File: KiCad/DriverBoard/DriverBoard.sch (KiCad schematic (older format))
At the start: 14 parts, among them J1 Conn_01x11, J2 Conn_01x05, J4 Conn_01x12, Q1 Q_DUAL_NPN_PNP_BRT_E1B1C2E2B2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, Q2 Q_DUAL_NPN_PNP_BRT_E1B1C2E2B2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, Q3 Q_DUAL_NPN_PNP_BRT_E1B1C2E2B2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, Q4 Q_DUAL_NPN_PNP_BRT_E1B1C2E2B2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, Q5 Q_DUAL_NPN_PNP_BRT_E1B1C2E2B2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, Q6 Q_DUAL_NPN_PNP_BRT_E1B1C2E2B2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, Q7 Q_DUAL_NPN_PNP_BRT_E1B1C2E2B2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

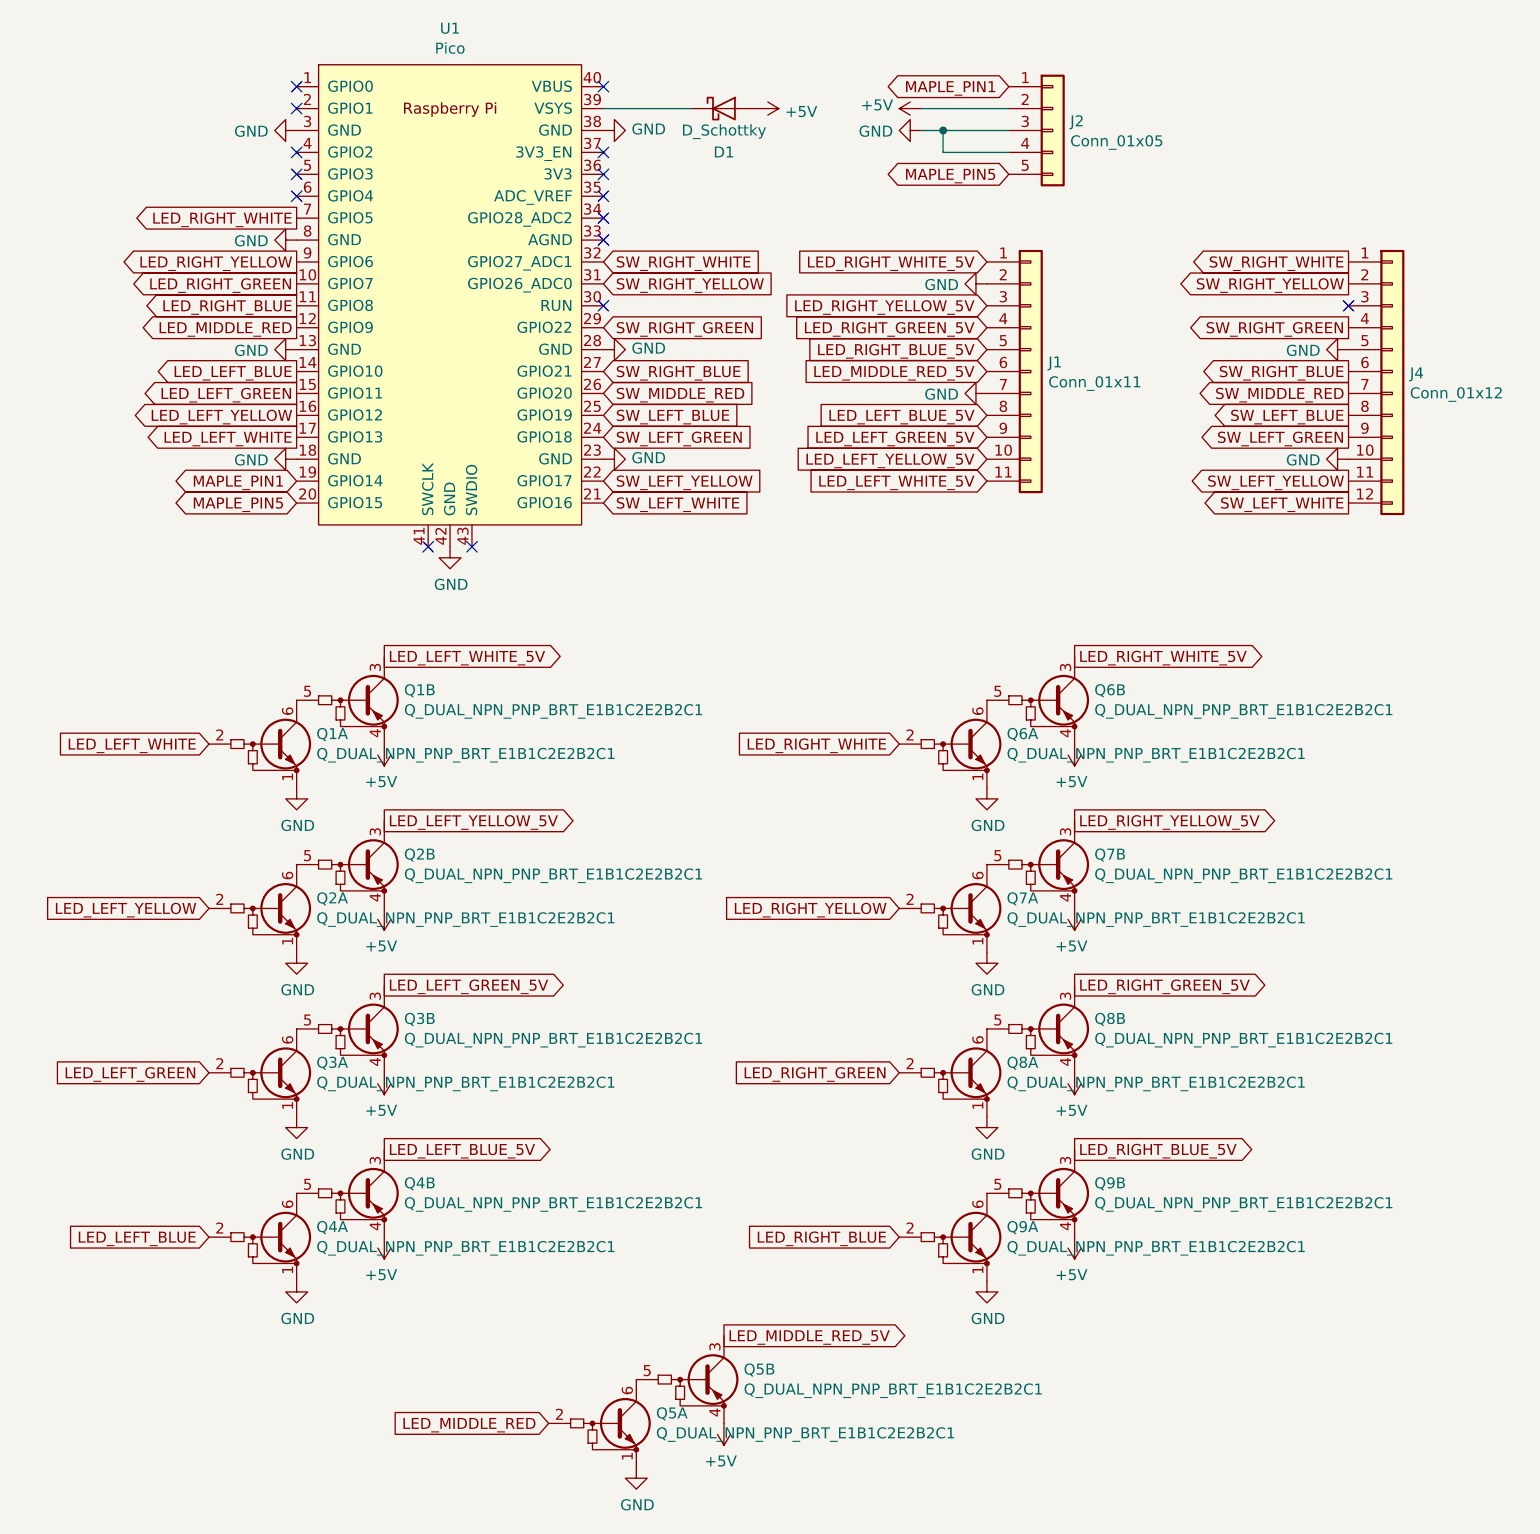
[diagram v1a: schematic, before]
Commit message: Switched misleading silkscreen and updated part numbers
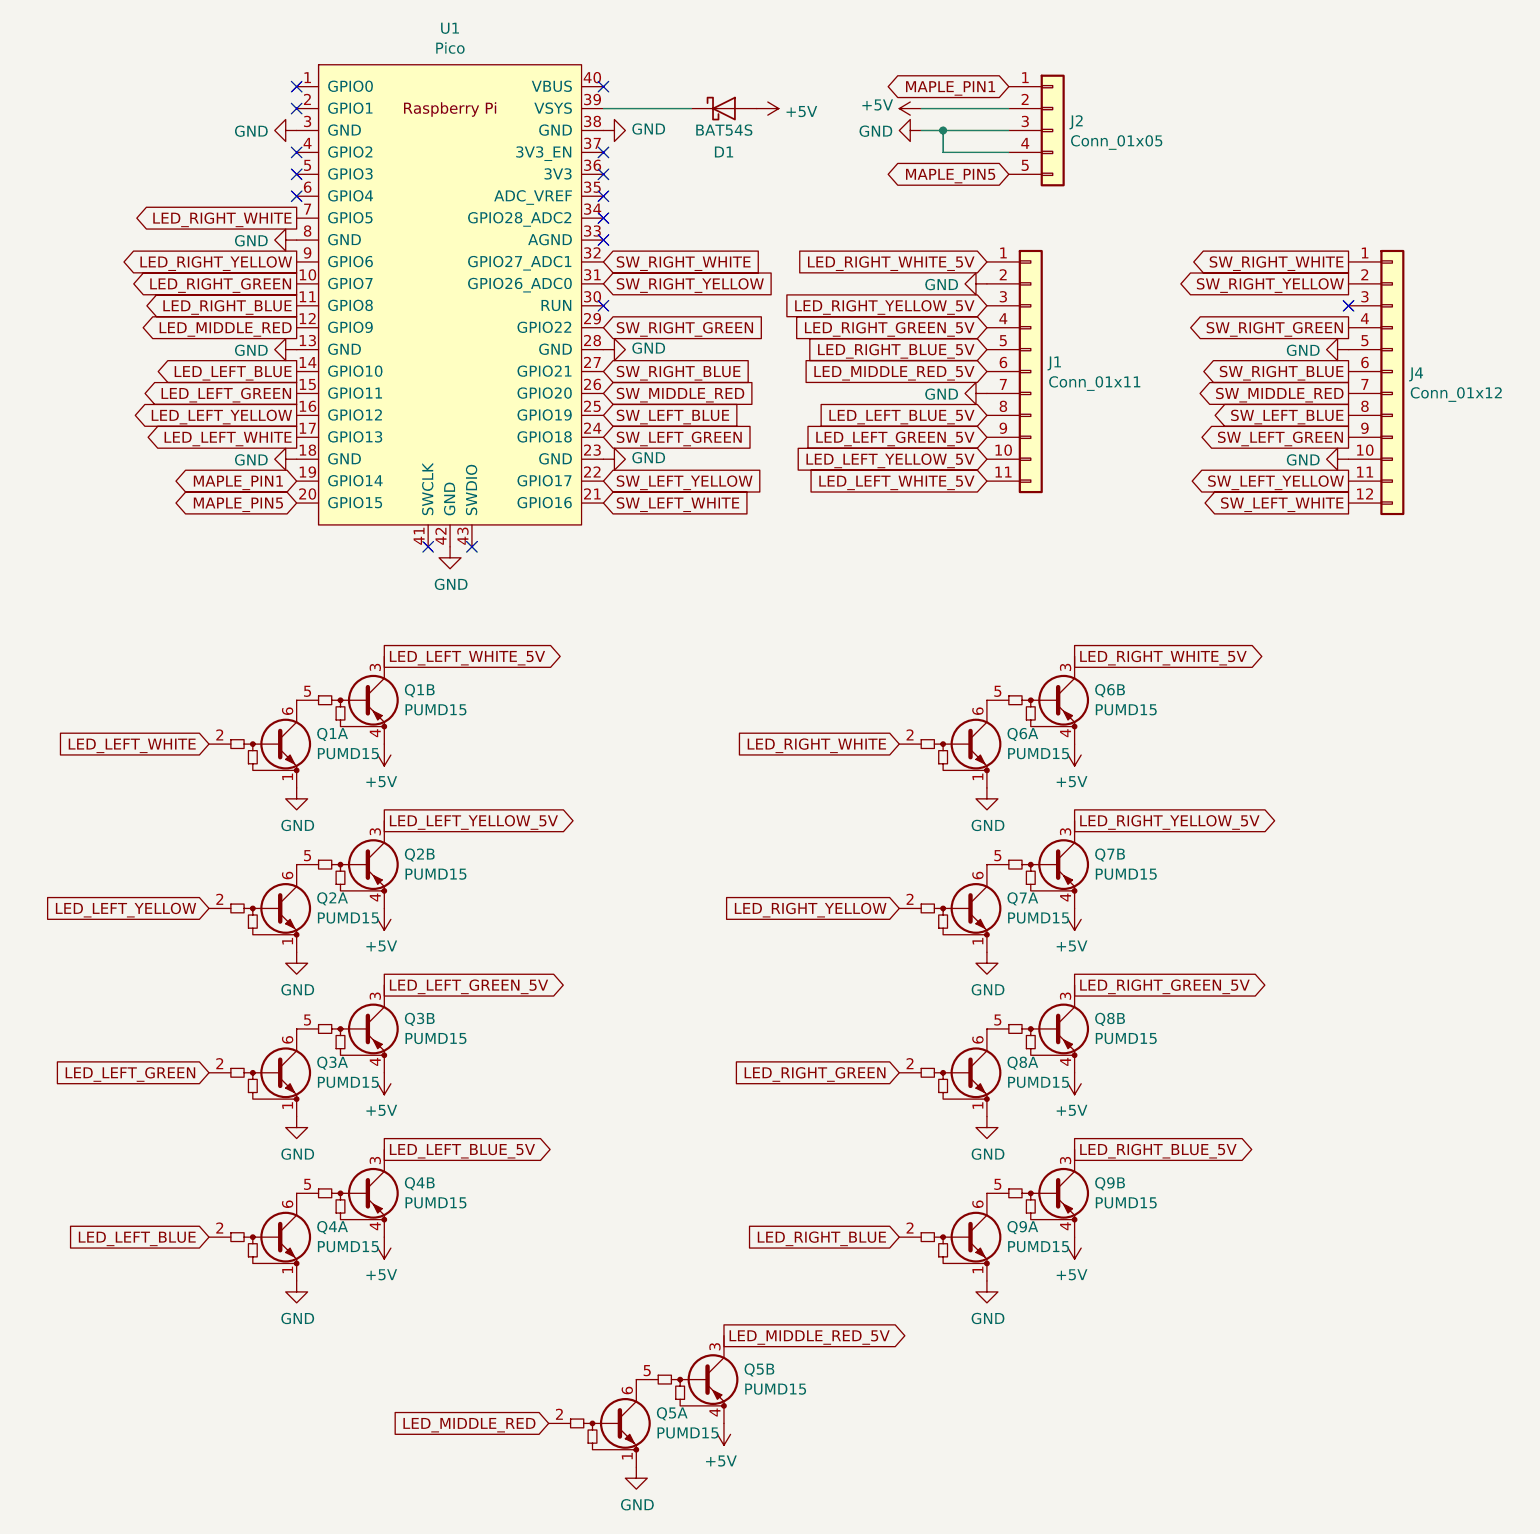
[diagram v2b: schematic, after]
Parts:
- D1: value D_Schottky -> BAT54S
- Q1, Q2, Q3, Q4, Q5, Q6, Q7, Q8, Q9: value Q_DUAL_NPN_PNP_BRT_E1B1C2E2B2C1 -> PUMD15
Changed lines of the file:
@@
 P 3750 1300
 F 0 "D1" H 3750 1100 50  0000 C CNN
-F 1 "D_Schottky" H 3750 1200 50  0000 C CNN
+F 1 "BAT54S" H 3750 1200 50  0000 C CNN
 F 2 "Diode_SMD:D_SOT-23_ANK" H 3750 1300 50  0001 C CNN
-F 3 "~" H 3750 1300 50  0001 C CNN
+F 3 "https://www.vishay.com/docs/85508/bat54.pdf" H 3750 1300 50  0001 C CNN
 	1    3750 1300
 	1    0    0    -1
@@
 NoConn ~ 3200 1200
 $Comp
-L Device:Q_DUAL_NPN_PNP_BRT_E1B1C2E2B2C1 Q1
-U 1 1 6043FA1D
-P 1750 4200
-F 0 "Q1" H 1890 4246 50  0000 L CNN
-F 1 "Q_DUAL_NPN_PNP_BRT_E1B1C2E2B2C1" H 1890 4155 50  0000 L CNN
-F 2 "Package_TO_SOT_SMD:SOT-363_SC-70-6_Handsoldering" H 1750 4200 50  0001 C CNN
-F 3 "~" H 1750 4200 50  0001 C CNN
-	1    1750 4200
-	1    0    0    -1
-$EndComp
-$Comp
 L power:GND #PWR01
 U 1 1 6044CCD8
@@
 LED_LEFT_WHITE_5V
 $Comp
-L Device:Q_DUAL_NPN_PNP_BRT_E1B1C2E2B2C1 Q1
-U 2 1 60452943
-P 2150 4000
-F 0 "Q1" H 2290 4046 50  0000 L CNN
-F 1 "Q_DUAL_NPN_PNP_BRT_E1B1C2E2B2C1" H 2290 3955 50  0000 L CNN
-F 2 "Package_TO_SOT_SMD:SOT-363_SC-70-6_Handsoldering" H 2150 4000 50  0001 C CNN
-F 3 "~" H 2150 4000 50  0001 C CNN
-	2    2150 4000
-	1    0    0    -1
-$EndComp
-$Comp
 L power:GND #PWR02
 U 1 1 6045294F
@@
 P 1750 6450
 F 0 "Q4" H 1890 6496 50  0000 L CNN
-F 1 "Q_DUAL_NPN_PNP_BRT_E1B1C2E2B2C1" H 1890 6405 50  0000 L CNN
+F 1 "PUMD15" H 1890 6405 50  0000 L CNN
 F 2 "Package_TO_SOT_SMD:SOT-363_SC-70-6_Handsoldering" H 1750 6450 50  0001 C CNN
-F 3 "~" H 1750 6450 50  0001 C CNN
+F 3 "https://docs.rs-online.com/2f69/0900766b8061d53b.pdf" H 1750 6450 50  0001 C CNN
 	1    1750 6450
 	1    0    0    -1
@@
 P 2150 4750
 F 0 "Q2" H 2290 4796 50  0000 L CNN
-F 1 "Q_DUAL_NPN_PNP_BRT_E1B1C2E2B2C1" H 2290 4705 50  0000 L CNN
+F 1 "PUMD15" H 2290 4705 50  0000 L CNN
 F 2 "Package_TO_SOT_SMD:SOT-363_SC-70-6_Handsoldering" H 2150 4750 50  0001 C CNN
-F 3 "~" H 2150 4750 50  0001 C CNN
+F 3 "https://docs.rs-online.com/2f69/0900766b8061d53b.pdf" H 2150 4750 50  0001 C CNN
 	2    2150 4750
 	1    0    0    -1
@@
 P 2150 6250
 F 0 "Q4" H 2290 6296 50  0000 L CNN
-F 1 "Q_DUAL_NPN_PNP_BRT_E1B1C2E2B2C1" H 2290 6205 50  0000 L CNN
+F 1 "PUMD15" H 2290 6205 50  0000 L CNN
 F 2 "Package_TO_SOT_SMD:SOT-363_SC-70-6_Handsoldering" H 2150 6250 50  0001 C CNN
-F 3 "~" H 2150 6250 50  0001 C CNN
+F 3 "https://docs.rs-online.com/2f69/0900766b8061d53b.pdf" H 2150 6250 50  0001 C CNN
 	2    2150 6250
 	1    0    0    -1
@@
 P 4900 4200
 F 0 "Q6" H 5040 4246 50  0000 L CNN
-F 1 "Q_DUAL_NPN_PNP_BRT_E1B1C2E2B2C1" H 5040 4155 50  0000 L CNN
+F 1 "PUMD15" H 5040 4155 50  0000 L CNN
 F 2 "Package_TO_SOT_SMD:SOT-363_SC-70-6_Handsoldering" H 4900 4200 50  0001 C CNN
-F 3 "~" H 4900 4200 50  0001 C CNN
+F 3 "https://docs.rs-online.com/2f69/0900766b8061d53b.pdf" H 4900 4200 50  0001 C CNN
 	1    4900 4200
 	1    0    0    -1
@@
 P 4900 5700
 F 0 "Q8" H 5040 5746 50  0000 L CNN
-F 1 "Q_DUAL_NPN_PNP_BRT_E1B1C2E2B2C1" H 5040 5655 50  0000 L CNN
+F 1 "PUMD15" H 5040 5655 50  0000 L CNN
 F 2 "Package_TO_SOT_SMD:SOT-363_SC-70-6_Handsoldering" H 4900 5700 50  0001 C CNN
-F 3 "~" H 4900 5700 50  0001 C CNN
+F 3 "https://docs.rs-online.com/2f69/0900766b8061d53b.pdf" H 4900 5700 50  0001 C CNN
 	1    4900 5700
 	1    0    0    -1
@@
 P 5300 4000
 F 0 "Q6" H 5440 4046 50  0000 L CNN
-F 1 "Q_DUAL_NPN_PNP_BRT_E1B1C2E2B2C1" H 5440 3955 50  0000 L CNN
+F 1 "PUMD15" H 5440 3955 50  0000 L CNN
 F 2 "Package_TO_SOT_SMD:SOT-363_SC-70-6_Handsoldering" H 5300 4000 50  0001 C CNN
-F 3 "~" H 5300 4000 50  0001 C CNN
+F 3 "https://docs.rs-online.com/2f69/0900766b8061d53b.pdf" H 5300 4000 50  0001 C CNN
 	2    5300 4000
 	1    0    0    -1
@@
 P 5300 5500
 F 0 "Q8" H 5440 5546 50  0000 L CNN
-F 1 "Q_DUAL_NPN_PNP_BRT_E1B1C2E2B2C1" H 5440 5455 50  0000 L CNN
+F 1 "PUMD15" H 5440 5455 50  0000 L CNN
 F 2 "Package_TO_SOT_SMD:SOT-363_SC-70-6_Handsoldering" H 5300 5500 50  0001 C CNN
-F 3 "~" H 5300 5500 50  0001 C CNN
+F 3 "https://docs.rs-online.com/2f69/0900766b8061d53b.pdf" H 5300 5500 50  0001 C CNN
 	2    5300 5500
 	1    0    0    -1
@@
 P 4900 4950
 F 0 "Q7" H 5040 4996 50  0000 L CNN
-F 1 "Q_DUAL_NPN_PNP_BRT_E1B1C2E2B2C1" H 5040 4905 50  0000 L CNN
+F 1 "PUMD15" H 5040 4905 50  0000 L CNN
 F 2 "Package_TO_SOT_SMD:SOT-363_SC-70-6_Handsoldering" H 4900 4950 50  0001 C CNN
-F 3 "~" H 4900 4950 50  0001 C CNN
+F 3 "https://docs.rs-online.com/2f69/0900766b8061d53b.pdf" H 4900 4950 50  0001 C CNN
 	1    4900 4950
 	1    0    0    -1
@@
 P 4900 6450
 F 0 "Q9" H 5040 6496 50  0000 L CNN
-F 1 "Q_DUAL_NPN_PNP_BRT_E1B1C2E2B2C1" H 5040 6405 50  0000 L CNN
+F 1 "PUMD15" H 5040 6405 50  0000 L CNN
 F 2 "Package_TO_SOT_SMD:SOT-363_SC-70-6_Handsoldering" H 4900 6450 50  0001 C CNN
-F 3 "~" H 4900 6450 50  0001 C CNN
+F 3 "https://docs.rs-online.com/2f69/0900766b8061d53b.pdf" H 4900 6450 50  0001 C CNN
 	1    4900 6450
 	1    0    0    -1
@@
 P 5300 4750
 F 0 "Q7" H 5440 4796 50  0000 L CNN
-F 1 "Q_DUAL_NPN_PNP_BRT_E1B1C2E2B2C1" H 5440 4705 50  0000 L CNN
+F 1 "PUMD15" H 5440 4705 50  0000 L CNN
 F 2 "Package_TO_SOT_SMD:SOT-363_SC-70-6_Handsoldering" H 5300 4750 50  0001 C CNN
-F 3 "~" H 5300 4750 50  0001 C CNN
+F 3 "https://docs.rs-online.com/2f69/0900766b8061d53b.pdf" H 5300 4750 50  0001 C CNN
 	2    5300 4750
 	1    0    0    -1
@@
 P 5300 6250
 F 0 "Q9" H 5440 6296 50  0000 L CNN
-F 1 "Q_DUAL_NPN_PNP_BRT_E1B1C2E2B2C1" H 5440 6205 50  0000 L CNN
+F 1 "PUMD15" H 5440 6205 50  0000 L CNN
 F 2 "Package_TO_SOT_SMD:SOT-363_SC-70-6_Handsoldering" H 5300 6250 50  0001 C CNN
-F 3 "~" H 5300 6250 50  0001 C CNN
+F 3 "https://docs.rs-online.com/2f69/0900766b8061d53b.pdf" H 5300 6250 50  0001 C CNN
 	2    5300 6250
 	1    0    0    -1
@@
 P 3300 7300
 F 0 "Q5" H 3440 7346 50  0000 L CNN
-F 1 "Q_DUAL_NPN_PNP_BRT_E1B1C2E2B2C1" H 3440 7255 50  0000 L CNN
+F 1 "PUMD15" H 3440 7255 50  0000 L CNN
 F 2 "Package_TO_SOT_SMD:SOT-363_SC-70-6_Handsoldering" H 3300 7300 50  0001 C CNN
-F 3 "~" H 3300 7300 50  0001 C CNN
+F 3 "https://docs.rs-online.com/2f69/0900766b8061d53b.pdf" H 3300 7300 50  0001 C CNN
 	1    3300 7300
 	1    0    0    -1
@@
 P 3700 7100
 F 0 "Q5" H 3840 7146 50  0000 L CNN
-F 1 "Q_DUAL_NPN_PNP_BRT_E1B1C2E2B2C1" H 3840 7055 50  0000 L CNN
+F 1 "PUMD15" H 3840 7055 50  0000 L CNN
 F 2 "Package_TO_SOT_SMD:SOT-363_SC-70-6_Handsoldering" H 3700 7100 50  0001 C CNN
-F 3 "~" H 3700 7100 50  0001 C CNN
+F 3 "https://docs.rs-online.com/2f69/0900766b8061d53b.pdf" H 3700 7100 50  0001 C CNN
 	2    3700 7100
 	1    0    0    -1
@@
 P 1750 4950
 F 0 "Q2" H 1890 4996 50  0000 L CNN
-F 1 "Q_DUAL_NPN_PNP_BRT_E1B1C2E2B2C1" H 1890 4905 50  0000 L CNN
+F 1 "PUMD15" H 1890 4905 50  0000 L CNN
 F 2 "Package_TO_SOT_SMD:SOT-363_SC-70-6_Handsoldering" H 1750 4950 50  0001 C CNN
-F 3 "~" H 1750 4950 50  0001 C CNN
+F 3 "https://docs.rs-online.com/2f69/0900766b8061d53b.pdf" H 1750 4950 50  0001 C CNN
 	1    1750 4950
 	1    0    0    -1
@@
 P 2150 5500
 F 0 "Q3" H 2290 5546 50  0000 L CNN
-F 1 "Q_DUAL_NPN_PNP_BRT_E1B1C2E2B2C1" H 2290 5455 50  0000 L CNN
+F 1 "PUMD15" H 2290 5455 50  0000 L CNN
 F 2 "Package_TO_SOT_SMD:SOT-363_SC-70-6_Handsoldering" H 2150 5500 50  0001 C CNN
-F 3 "~" H 2150 5500 50  0001 C CNN
+F 3 "https://docs.rs-online.com/2f69/0900766b8061d53b.pdf" H 2150 5500 50  0001 C CNN
 	2    2150 5500
 	1    0    0    -1
@@
 P 1750 5700
 F 0 "Q3" H 1890 5746 50  0000 L CNN
-F 1 "Q_DUAL_NPN_PNP_BRT_E1B1C2E2B2C1" H 1890 5655 50  0000 L CNN
+F 1 "PUMD15" H 1890 5655 50  0000 L CNN
 F 2 "Package_TO_SOT_SMD:SOT-363_SC-70-6_Handsoldering" H 1750 5700 50  0001 C CNN
-F 3 "~" H 1750 5700 50  0001 C CNN
+F 3 "https://docs.rs-online.com/2f69/0900766b8061d53b.pdf" H 1750 5700 50  0001 C CNN
 	1    1750 5700
 	1    0    0    -1
 $EndComp
 NoConn ~ 3200 1800
+$Comp
+L Device:Q_DUAL_NPN_PNP_BRT_E1B1C2E2B2C1 Q1
+U 1 1 6043FA1D
+P 1750 4200
+F 0 "Q1" H 1890 4246 50  0000 L CNN
+F 1 "PUMD15" H 1890 4155 50  0000 L CNN
+F 2 "Package_TO_SOT_SMD:SOT-363_SC-70-6_Handsoldering" H 1750 4200 50  0001 C CNN
+F 3 "https://docs.rs-online.com/2f69/0900766b8061d53b.pdf" H 1750 4200 50  0001 C CNN
+	1    1750 4200
+	1    0    0    -1
+$EndComp
+$Comp
+L Device:Q_DUAL_NPN_PNP_BRT_E1B1C2E2B2C1 Q1
+U 2 1 60452943
+P 2150 4000
+F 0 "Q1" H 2290 4046 50  0000 L CNN
+F 1 "PUMD15" H 2290 3955 50  0000 L CNN
+F 2 "Package_TO_SOT_SMD:SOT-363_SC-70-6_Handsoldering" H 2150 4000 50  0001 C CNN
+F 3 "https://docs.rs-online.com/2f69/0900766b8061d53b.pdf" H 2150 4000 50  0001 C CNN
+	2    2150 4000
+	1    0    0    -1
+$EndComp
 $EndSCHEMATC
